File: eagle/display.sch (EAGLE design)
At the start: 40 parts, among them IC5 APX803, P1IN TPTP10R, P1RET TPTP10R, P2IN TPTP10R, P2RET TPTP10R, P3IN TPTP10R, P3RET TPTP10R, P4IN TPTP10R, Q1 MMBT2222, T1 BC846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

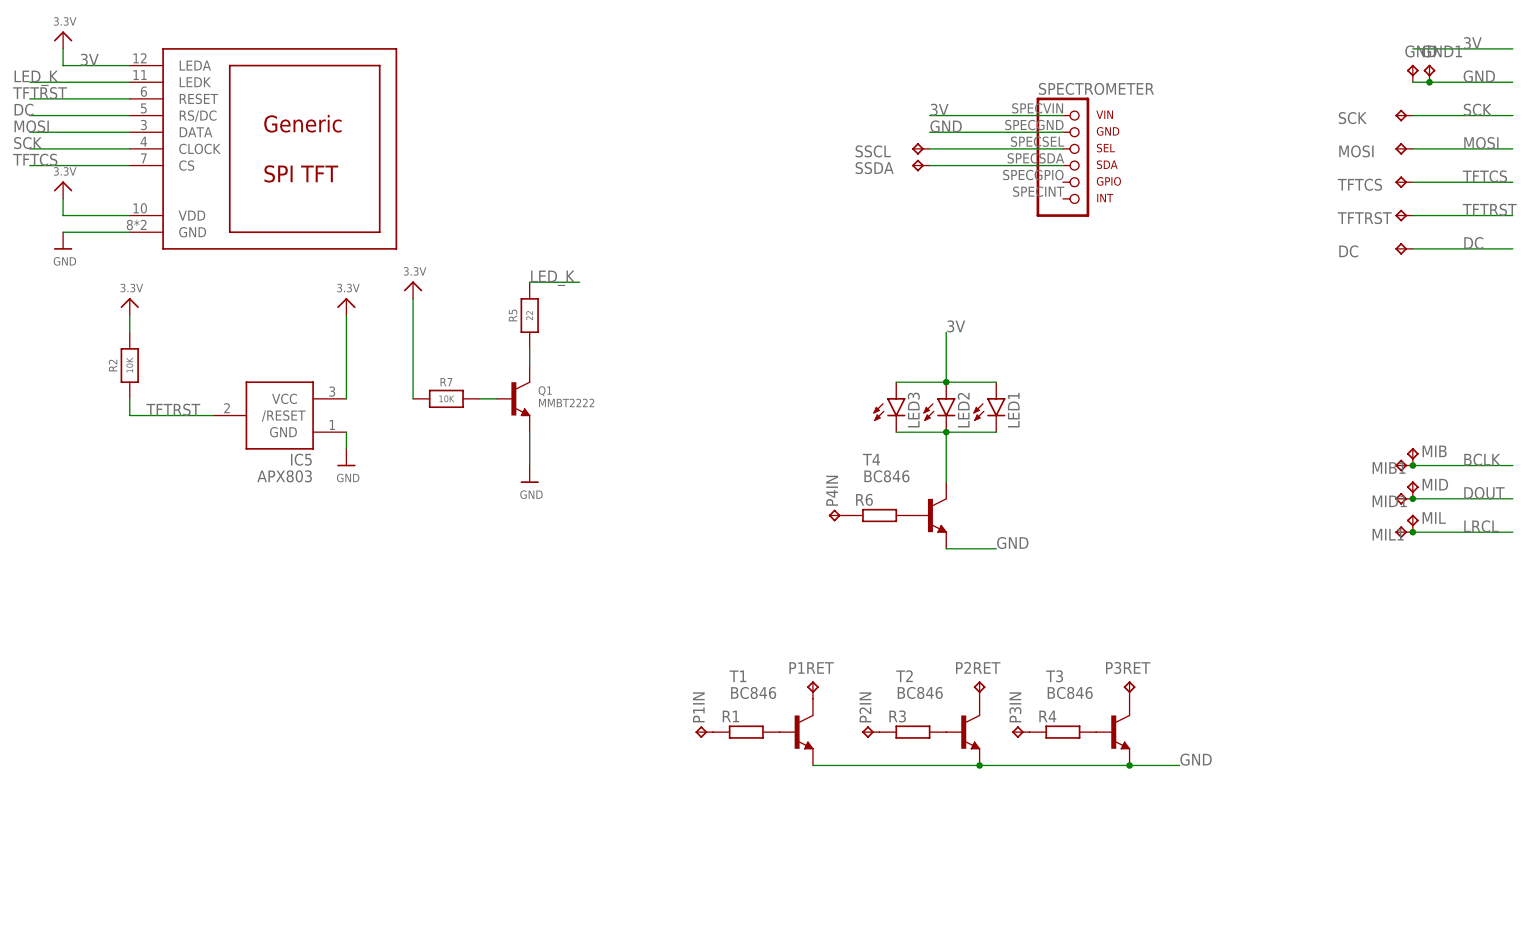
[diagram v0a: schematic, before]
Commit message: Display board redesigned with FFC connector
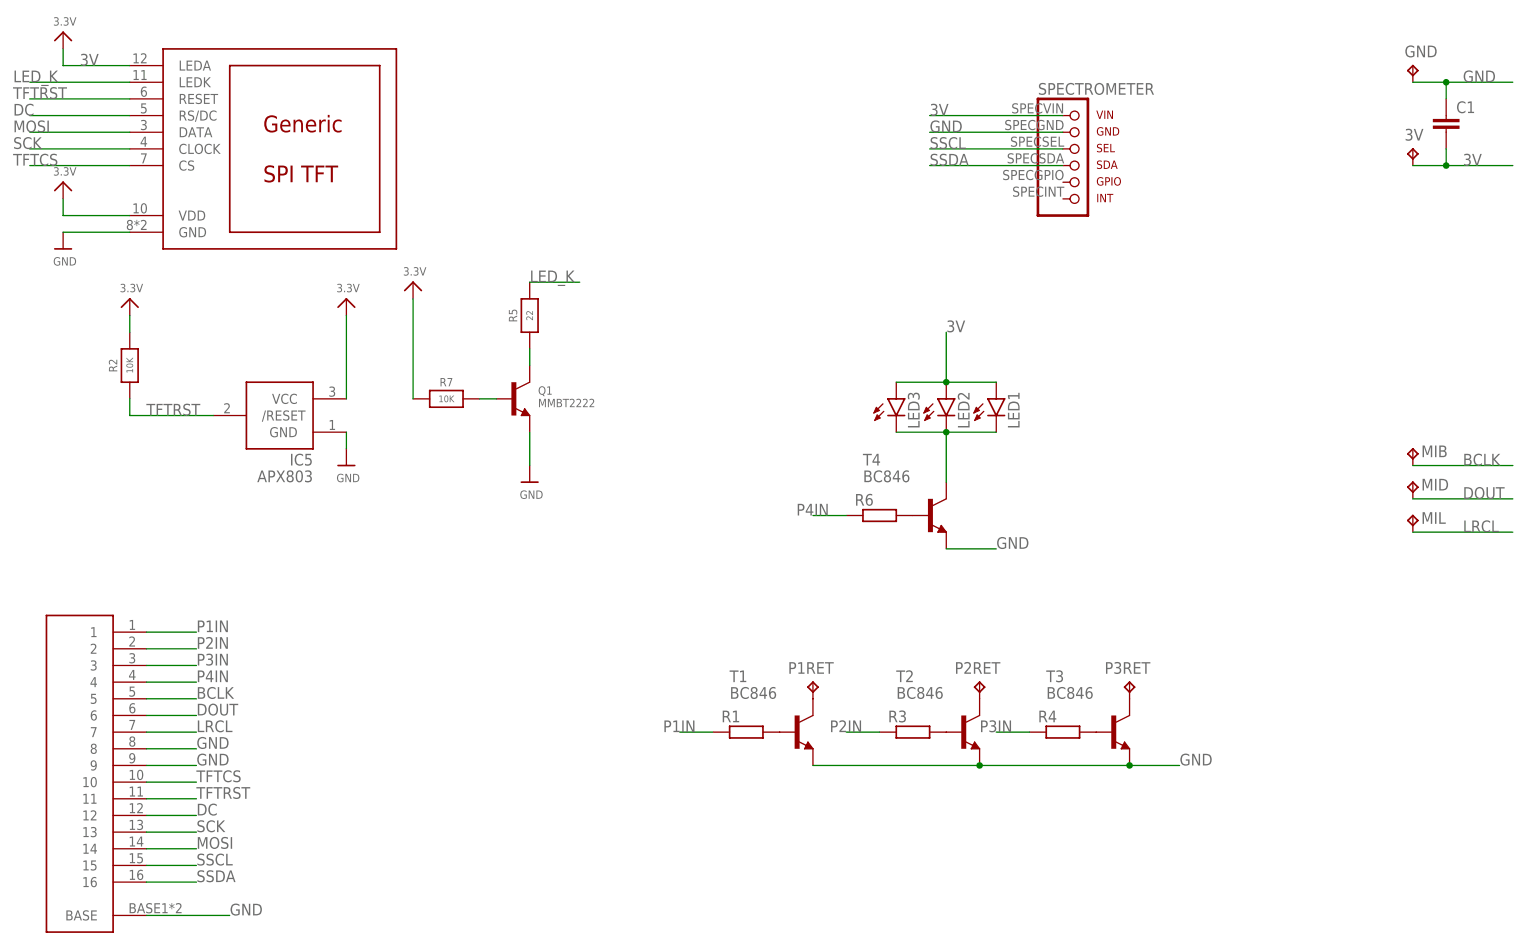
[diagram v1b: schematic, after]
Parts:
- removed DC, MIB1, MID1, MIL1, MOSI, P1IN, P2IN, P3IN, P4IN, SCK, SSCL, SSDA, TFTCS, TFTRST: TPTP10R, testpad:TPTP10R
- removed GND1: TPTP20R, testpad:TPTP20R
- added 3V: TPTP20R, testpad:TPTP20R
- added C1: (no value), resistor:C-EUC0805
- added U$3: 16PINFFC, general:16PINFFC
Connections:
- removed net N$11: P1IN.TP, R1.1
- removed net N$12: P2IN.TP, R3.1
- removed net N$13: P3IN.TP, R4.1
- removed net N$16: P4IN.TP, R6.1
- removed net N$2: SSCL.TP, U$2.SPECSEL
- removed net N$3: SSDA.TP, U$2.SPECSDA
- new net P1IN: R1.1, U$3.1
- new net P2IN: R3.1, U$3.2
- new net P3IN: R4.1, U$3.3
- new net P4IN: R6.1, U$3.4
- new net SSCL: U$2.SPECSEL, U$3.15
- new net SSDA: U$2.SPECSDA, U$3.16
- net 3V: now also 3V.TP, C1.2
- net BCLK: now also U$3.5; no longer MIB1.TP
- net DC: now also U$3.12; no longer DC.TP
- net DOUT: now also U$3.6; no longer MID1.TP
- net GND: now also C1.1, U$3.8, U$3.9, U$3.BASE; no longer GND1.TP
- net LRCL: now also U$3.7; no longer MIL1.TP
- net MOSI: now also U$3.14; no longer MOSI.TP
- net SCK: now also U$3.13; no longer SCK.TP
- net TFTCS: now also U$3.10; no longer TFTCS.TP
- net TFTRST: now also U$3.11; no longer TFTRST.TP
